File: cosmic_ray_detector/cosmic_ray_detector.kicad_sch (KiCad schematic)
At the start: 11 parts, among them J1 MOLEX micro-fit 43045-0210, J2 5 pin pin header, J3 Black Banana, J4 Red Banana, J5 Green Banana, J6 BNC

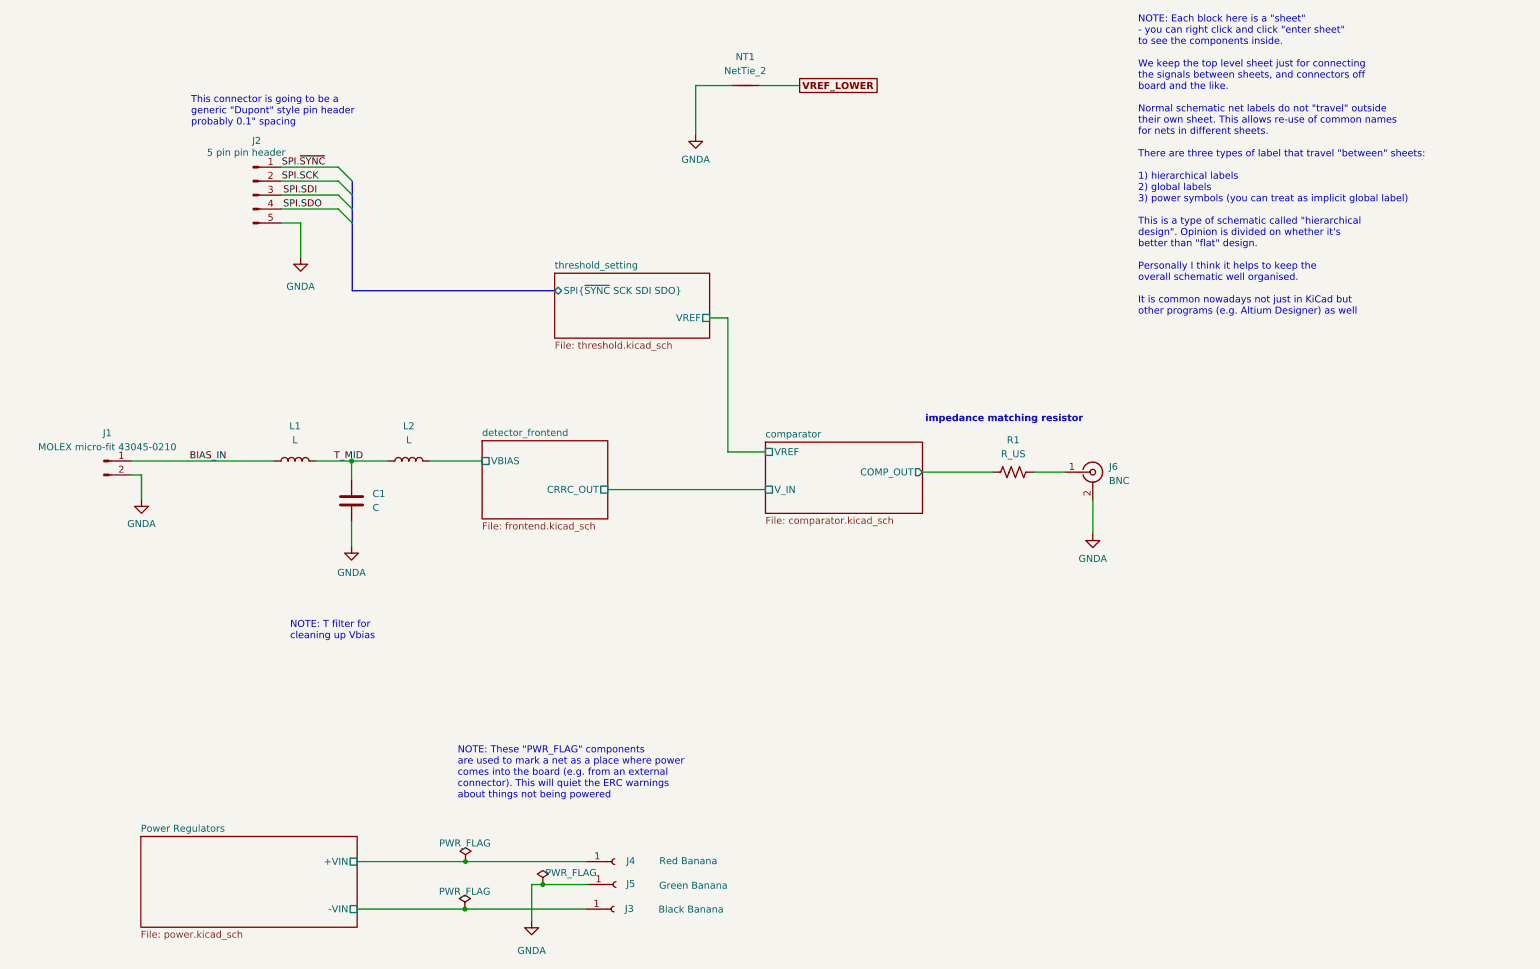
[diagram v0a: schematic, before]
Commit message: changed a couple more caps
all components reasonably grouped, almost placed
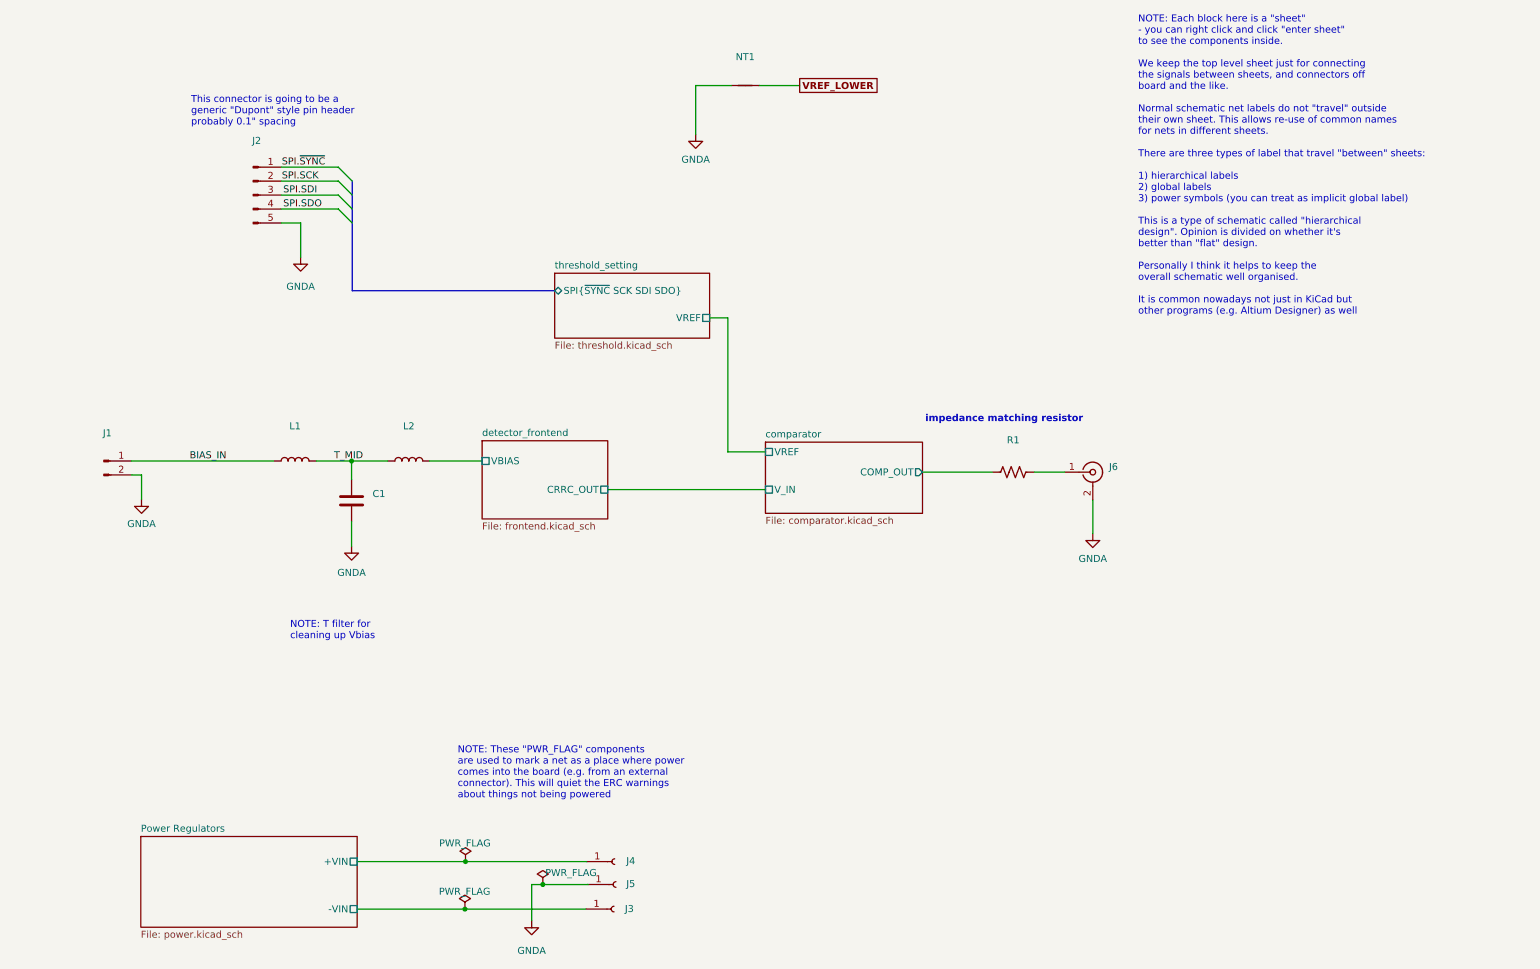
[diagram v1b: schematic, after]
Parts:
- C1: value C -> (none); footprint Capacitor_SMD:C_1210_3225Metric -> (none)
- J1: value MOLEX micro-fit 43045-0210 -> (none); footprint cosmic_ray_detector_lib:4304502_09 -> (none)
- J2: value 5 pin pin header -> (none); footprint Connector_PinHeader_1.27mm:PinHeader_1x05_P1.27mm_Vertical -> (none)
- J3: value Black Banana -> (none); footprint cosmic_ray_detector_lib:242432 -> (none)
- J4: value Red Banana -> (none); footprint cosmic_ray_detector_lib:242431 -> (none)
- J5: value Green Banana -> (none); footprint cosmic_ray_detector_lib:242434 -> (none)
- J6: value BNC -> (none); footprint cosmic_ray_detector_lib:MOLEX_731375003 -> (none)
- L1, L2: value L -> (none); footprint Inductor_SMD:L_1008_2520Metric -> (none)
- NT1: value NetTie_2 -> (none); footprint NetTie:NetTie-2_SMD_Pad0.5mm -> (none)
- R1: value R_US -> (none); footprint Resistor_SMD:R_0402_1005Metric -> (none)
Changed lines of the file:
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@@
     (in_bom yes) (on_board yes)
     (property "Reference" "J2" (id 0) (at 63.754 37.719 0))
-    (property "Value" "5 pin pin header" (id 1) (at 61.849 39.878 0))
-    (property "Footprint" "Connector_PinHeader_1.27mm:PinHeader_1x05_P1.27mm_Vertical" (id 2) (at 63.119 47.625 0)
+    (property "Value" "" (id 1) (at 61.849 39.878 0))
+    (property "Footprint" "" (id 2) (at 63.119 47.625 0)
       (effects (font (size 1.27 1.27)) hide)
     )
@@
       (effects (font (size 1.27 1.27)) (justify right))
     )
-    (property "Value" "C" (id 1) (at 84.836 104.5209 0)
-      (effects (font (size 1.27 1.27)) (justify right))
-    )
-    (property "Footprint" "Capacitor_SMD:C_1210_3225Metric" (id 2) (at 80.0608 99.441 0)
+    (property "Value" "" (id 1) (at 84.836 104.5209 0)
+      (effects (font (size 1.27 1.27)) (justify right))
+    )
+    (property "Footprint" "" (id 2) (at 80.0608 99.441 0)
       (effects (font (size 1.27 1.27)) hide)
     )
@@
       (effects (font (size 1.27 1.27)) (justify left))
     )
-    (property "Value" "BNC" (id 1) (at 218.8464 99.6071 0)
-      (effects (font (size 1.27 1.27)) (justify left))
-    )
-    (property "Footprint" "cosmic_ray_detector_lib:MOLEX_731375003" (id 2) (at 215.9 98.044 0)
+    (property "Value" "" (id 1) (at 218.8464 99.6071 0)
+      (effects (font (size 1.27 1.27)) (justify left))
+    )
+    (property "Footprint" "" (id 2) (at 215.9 98.044 0)
       (effects (font (size 1.27 1.27)) hide)
     )
@@
     (in_bom yes) (on_board yes) (fields_autoplaced)
     (property "Reference" "L1" (id 0) (at 70.739 89.662 90))
-    (property "Value" "L" (id 1) (at 70.739 92.202 90))
-    (property "Footprint" "Inductor_SMD:L_1008_2520Metric" (id 2) (at 70.739 96.012 0)
+    (property "Value" "" (id 1) (at 70.739 92.202 90))
+    (property "Footprint" "" (id 2) (at 70.739 96.012 0)
       (effects (font (size 1.27 1.27)) hide)
     )
@@
       (effects (font (size 1.27 1.27)) (justify left))
     )
-    (property "Value" "Red Banana" (id 1) (at 137.033 168.783 0)
-      (effects (font (size 1.27 1.27)) (justify left))
-    )
-    (property "Footprint" "cosmic_ray_detector_lib:242431" (id 2) (at 128.905 168.91 0)
+    (property "Value" "" (id 1) (at 137.033 168.783 0)
+      (effects (font (size 1.27 1.27)) (justify left))
+    )
+    (property "Footprint" "" (id 2) (at 128.905 168.91 0)
       (effects (font (size 1.27 1.27)) hide)
     )
@@
     (in_bom yes) (on_board yes) (fields_autoplaced)
     (property "Reference" "J1" (id 0) (at 36.576 90.932 0))
-    (property "Value" "MOLEX micro-fit 43045-0210" (id 1) (at 36.576 93.472 0))
-    (property "Footprint" "cosmic_ray_detector_lib:4304502_09" (id 2) (at 35.941 96.012 0)
+    (property "Value" "" (id 1) (at 36.576 93.472 0))
+    (property "Footprint" "" (id 2) (at 35.941 96.012 0)
       (effects (font (size 1.27 1.27)) hide)
     )
@@
     (in_bom yes) (on_board yes) (fields_autoplaced)
     (property "Reference" "L2" (id 0) (at 91.44 89.662 90))
-    (property "Value" "L" (id 1) (at 91.44 92.202 90))
-    (property "Footprint" "Inductor_SMD:L_1008_2520Metric" (id 2) (at 91.44 96.012 0)
+    (property "Value" "" (id 1) (at 91.44 92.202 90))
+    (property "Footprint" "" (id 2) (at 91.44 96.012 0)
       (effects (font (size 1.27 1.27)) hide)
     )
@@
       (effects (font (size 1.27 1.27)) (justify left))
     )
-    (property "Value" "Green Banana" (id 1) (at 136.9822 173.2534 0)
-      (effects (font (size 1.27 1.27)) (justify left))
-    )
-    (property "Footprint" "cosmic_ray_detector_lib:242434" (id 2) (at 129.1336 173.0756 0)
+    (property "Value" "" (id 1) (at 136.9822 173.2534 0)
+      (effects (font (size 1.27 1.27)) (justify left))
+    )
+    (property "Footprint" "" (id 2) (at 129.1336 173.0756 0)
       (effects (font (size 1.27 1.27)) hide)
     )
@@
     (in_bom yes) (on_board yes) (fields_autoplaced)
     (property "Reference" "NT1" (id 0) (at 152.654 22.479 0))
-    (property "Value" "NetTie_2" (id 1) (at 152.654 25.019 0))
-    (property "Footprint" "NetTie:NetTie-2_SMD_Pad0.5mm" (id 2) (at 152.654 27.686 0)
+    (property "Value" "" (id 1) (at 152.654 25.019 0))
+    (property "Footprint" "" (id 2) (at 152.654 27.686 0)
       (effects (font (size 1.27 1.27)) hide)
     )
@@
       (effects (font (size 1.27 1.27)) (justify left))
     )
-    (property "Value" "Black Banana" (id 1) (at 136.8552 177.5968 0)
-      (effects (font (size 1.27 1.27)) (justify left))
-    )
-    (property "Footprint" "cosmic_ray_detector_lib:242432" (id 2) (at 128.778 177.546 0)
+    (property "Value" "" (id 1) (at 136.8552 177.5968 0)
+      (effects (font (size 1.27 1.27)) (justify left))
+    )
+    (property "Footprint" "" (id 2) (at 128.778 177.546 0)
       (effects (font (size 1.27 1.27)) hide)
     )
@@
     (in_bom yes) (on_board yes) (fields_autoplaced)
     (property "Reference" "R1" (id 0) (at 201.422 92.202 90))
-    (property "Value" "R_US" (id 1) (at 201.422 94.742 90))
-    (property "Footprint" "Resistor_SMD:R_0402_1005Metric" (id 2) (at 201.676 97.028 90)
+    (property "Value" "" (id 1) (at 201.422 94.742 90))
+    (property "Footprint" "" (id 2) (at 201.676 97.028 90)
       (effects (font (size 1.27 1.27)) hide)
     )
@@
     )
     (path "/6f9e921d-fe8f-4a5a-8c5c-cbe4afe99abc/b8ce0ab1-12e9-4729-8cf0-b6c9aa72ce7b"
-      (reference "C2") (unit 1) (value "10uF") (footprint "cosmic_ray_detector_lib:MAL215375109E3")
+      (reference "C2") (unit 1) (value "10uF") (footprint "Capacitor_Tantalum_SMD:CP_EIA-3216-12_Kemet-S")
     )
     (path "/6f9e921d-fe8f-4a5a-8c5c-cbe4afe99abc/9342db19-454a-448f-a9b0-e083f29fdbc6"
-      (reference "C3") (unit 1) (value "10uF") (footprint "cosmic_ray_detector_lib:MAL215375109E3")
+      (reference "C3") (unit 1) (value "10uF") (footprint "Capacitor_Tantalum_SMD:CP_EIA-3216-12_Kemet-S")
     )
     (path "/6f9e921d-fe8f-4a5a-8c5c-cbe4afe99abc/64d6d08c-f5e1-413e-9e3e-c0a6aeb2fc5f"

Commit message: update routed / finished PCB to version 9
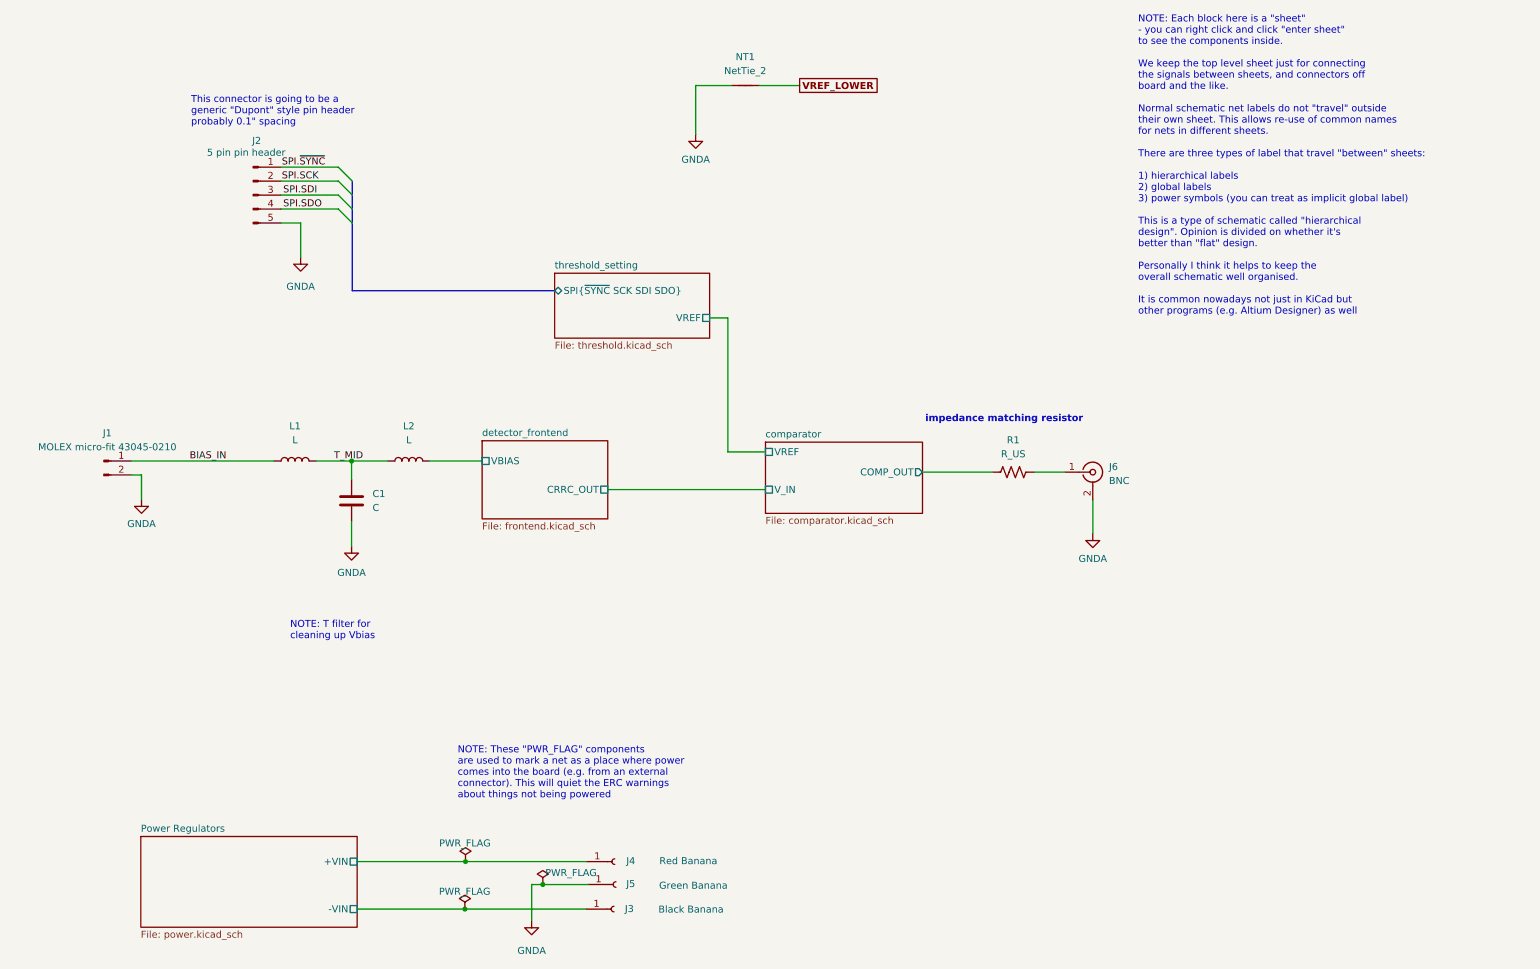
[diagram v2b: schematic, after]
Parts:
- C1: value (none) -> C; footprint (none) -> Capacitor_SMD:C_1210_3225Metric
- J1: value (none) -> MOLEX micro-fit 43045-0210; footprint (none) -> cosmic_ray_detector_lib:4304502_09
- J2: value (none) -> 5 pin pin header; footprint (none) -> Connector_PinHeader_1.27mm:PinHeader_1x05_P1.27mm_Vertical
- J3: value (none) -> Black Banana; footprint (none) -> cosmic_ray_detector_lib:242432
- J4: value (none) -> Red Banana; footprint (none) -> cosmic_ray_detector_lib:242431
- J5: value (none) -> Green Banana; footprint (none) -> cosmic_ray_detector_lib:242434
- J6: value (none) -> BNC; footprint (none) -> cosmic_ray_detector_lib:MOLEX_731375003
- L1, L2: value (none) -> L; footprint (none) -> Inductor_SMD:L_1008_2520Metric
- NT1: value (none) -> NetTie_2; footprint (none) -> NetTie:NetTie-2_SMD_Pad0.5mm
- R1: value (none) -> R_US; footprint (none) -> Resistor_SMD:R_0402_1005Metric

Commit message: update pcb and schem to V10
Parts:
- added TP4: TestPoint, cosmic_ray_detector_lib:harwin_tp_SMD, symbol Connector:TestPoint
- J1: symbol Connector:Conn_01x02_Male -> Connector:Conn_01x02_Pin
- J2: symbol Connector:Conn_01x05_Male -> Connector:Conn_01x05_Pin
- J3, J4, J5: symbol Connector:Conn_01x01_Female -> Connector:Conn_01x01_Socket
- R1: footprint Resistor_SMD:R_0402_1005Metric -> cosmic_ray_detector_lib:R_0402_1005Metric
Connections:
- net GNDA: now also TP4.1
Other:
- moved on the sheet: J1, J2, J3, J4, J5, L1, L2, R1

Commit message: update incomplete schem branch for V10
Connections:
- net detector_frontend/VBIAS: no longer names the net of L2.2
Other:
- removed sheet detector_frontend
- note added: "PUT YOUR DETECTOR FRONTEND PAGE HERE!"
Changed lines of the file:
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@@
 		(comment 1 "design by: Dan Weatherill")
+	)
+	(rectangle
+		(start 112.776 92.202)
+		(end 142.494 114.046)
+		(stroke
+			(width 0)
+			(type dash)
+		)
+		(fill
+			(type none)
+		)
 	)
 	(text "NOTE: These \"PWR_FLAG\" components\nare used to mark a net as a place where power \ncomes into the board (e.g. from an external\nconnector). This will quiet the ERC warnings\nabout things not being powered"
@@
 			)
 			(justify left bottom)
+		)
+	)
+	(text "PUT YOUR DETECTOR \nFRONTEND PAGE HERE!"
+		(exclude_from_sim no)
+		(at 126.238 100.33 0)
+		(effects
+			(font
+				(size 1.27 1.27)
+				(thickness 0.254)
+				(bold yes)
+			)
 		)
 	)
@@
 		(pts
 			(xy 40.64 96.52) (xy 67.31 96.52)
-		)
-		(stroke
-			(width 0)
-			(type default)
-		)
-	)
-	(wire
-		(pts
-			(xy 128.27 101.6) (xy 156.21 101.6)
 		)
 		(stroke
@@
 				)
 			)
-		)
-	)
-	(sheet
-		(at 105.41 92.837)
-		(size 22.86 14.224)
-		(exclude_from_sim no)
-		(in_bom yes)
-		(on_board yes)
-		(dnp no)
-		(fields_autoplaced yes)
-		(stroke
-			(width 0.1524)
-			(type solid)
-		)
-		(fill
-			(color 0 0 0 0)
-		)
-		(property "Sheetname" "detector_frontend"
-			(at 105.41 92.1254 0)
-			(show_name no)
-			(do_not_autoplace no)
-			(effects
-				(font
-					(size 1.27 1.27)
-				)
-				(justify left bottom)
-			)
-		)
-		(property "Sheetfile" "frontend.kicad_sch"
-			(at 105.41 107.6456 0)
-			(show_name no)
-			(do_not_autoplace no)
-			(effects
-				(font
-					(size 1.27 1.27)
-				)
-				(justify left top)
-			)
-		)
-		(pin "VBIAS" passive
-			(at 105.41 96.52 180)
-			(effects
-				(font
-					(size 1.27 1.27)
-				)
-				(justify left)
-			)
-		)
-		(pin "CRRC_OUT" passive
-			(at 128.27 101.6 0)
-			(effects
-				(font
-					(size 1.27 1.27)
-				)
-				(justify right)
-			)
-		)
-		(instances
-			(project "cosmic_ray_detector"
-				(path "/f6c67f56-a7d8-40b4-925b-78738a0748d6"
-					(page "2")
-				)
-			)
